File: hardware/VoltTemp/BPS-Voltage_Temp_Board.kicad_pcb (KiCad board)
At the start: 2 copper layers, 98.2 x 56.2 mm, 144 parts, among them IC1 ISO1641BDR, J10 53307-2471, J11 Conn_01x07, J12 Conn_01x04, J13 Conn_01x04, J5 Logic_Analyzer, J6 Conn_01x04, J7 Conn_01x04, J8 Conn_01x06, J9 Conn_01x03, SW1 BOOT, U1 EL3H7, U12 TLV9062xD, U13 TLV9062xD, U14 TLV9062xD, U2 BQ7692003PW, U3 EL3H7, U4 TLV9062xD, U6 TLV9062xD

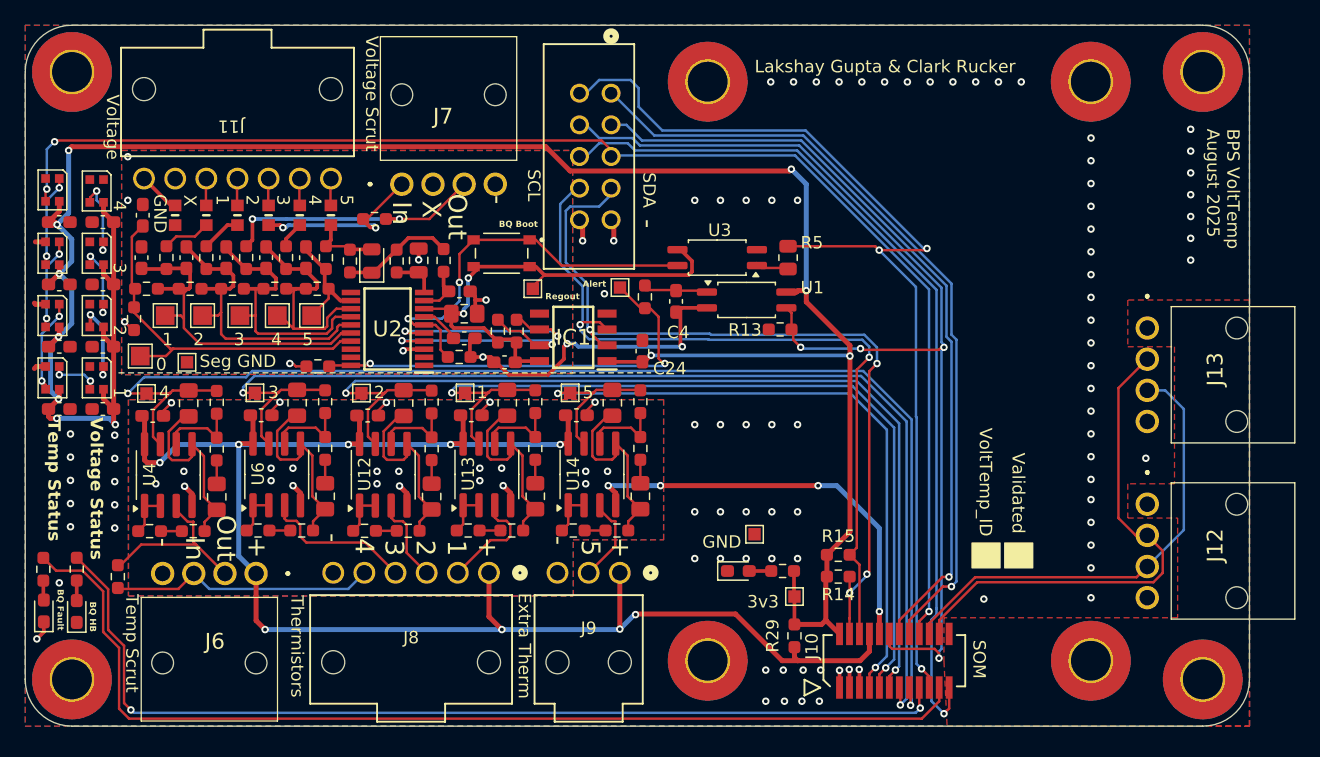
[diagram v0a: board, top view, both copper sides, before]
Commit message: fixed nanofit footprints and add labels to can in can out connectors
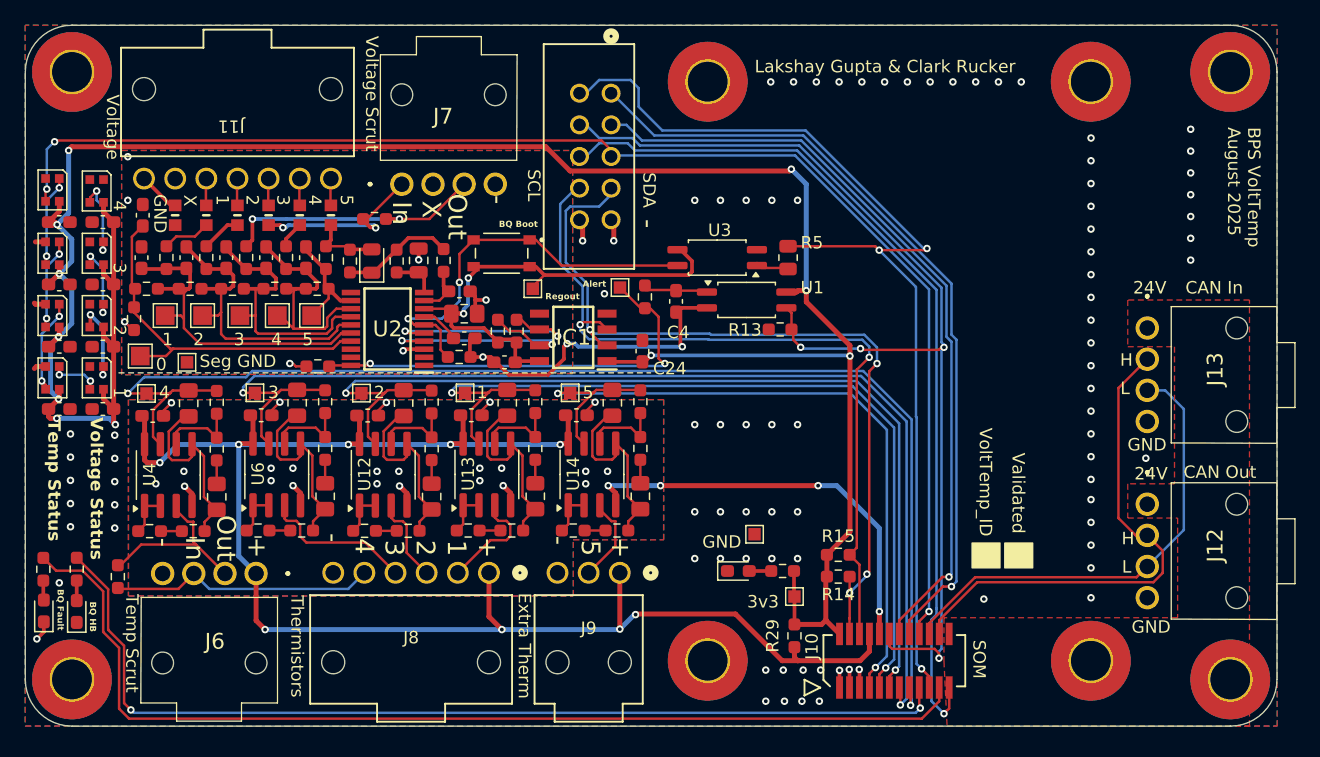
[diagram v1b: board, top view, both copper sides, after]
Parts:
- U2: value BQ7692003PW -> SOP65P640X120-20N
- moved MH4 2.21 mm to (215.0, 69.7)
- moved MH3 2.21 mm to (215.0, 118.4)
- moved LOGO2 0.43 mm to (209.4, 79.2)
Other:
- board size 98.2 x 56.2 mm -> 100.4 x 56.2 mm
- board text added: "24V"
- board text added: "CAN In"
- board text added: "CAN Out"
- board text added: "H"
- board text added: "L"
- board text added: "Todo: - Layout :( [X] - Update constrains [X] - Mirror thermistor flex pinout [X] - Label voltage connector [X] - Fix iso i2c footprint [X] - Make proper edge cuts [X] - Add stitching vias [X] - Update pcb from schematic once schematic todo done [X] - Figure out edge to connector clearance for nanofits [X] - Redo addressable led routing [X] - Verify 24V traces can handle 8 Volttemps of current [X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"
- board text removed: "Todo: - Layout :( [X] - Update constrains [X] - Mirror thermistor flex pinout [X] - Label voltage connector [X] - Fix iso i2c footprint [X] - Make proper edge cuts [X] - Add stitching vias [X] - Update pcb from schematic once schematic todo done [X] - Figure out edge to connector clearance for nanofits [] - Redo addressable led routing [X] - Verify 24V traces can handle 8 Volttemps of current [X]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"

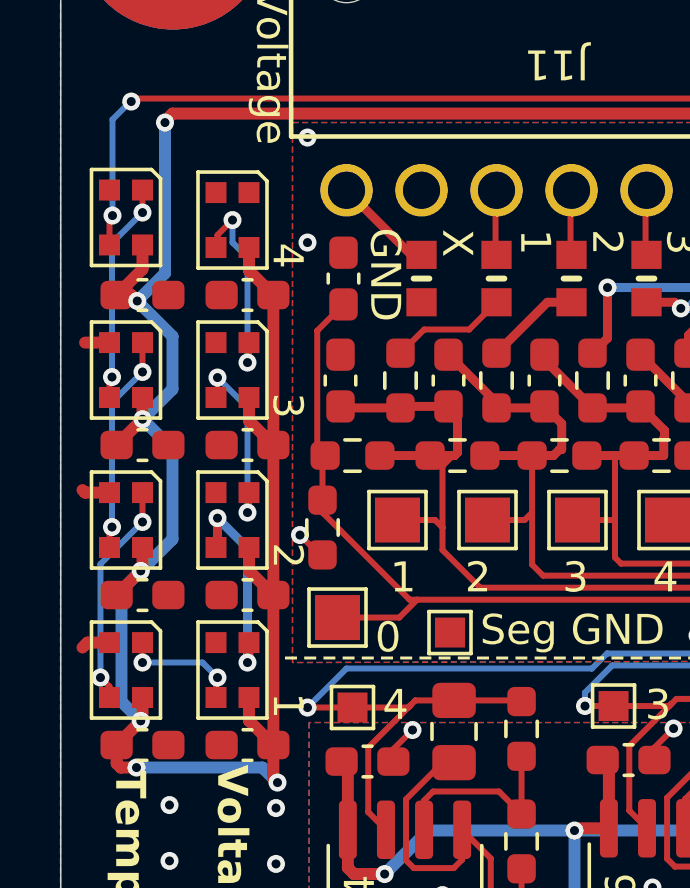
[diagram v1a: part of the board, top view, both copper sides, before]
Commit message: changed bild to sharepoint
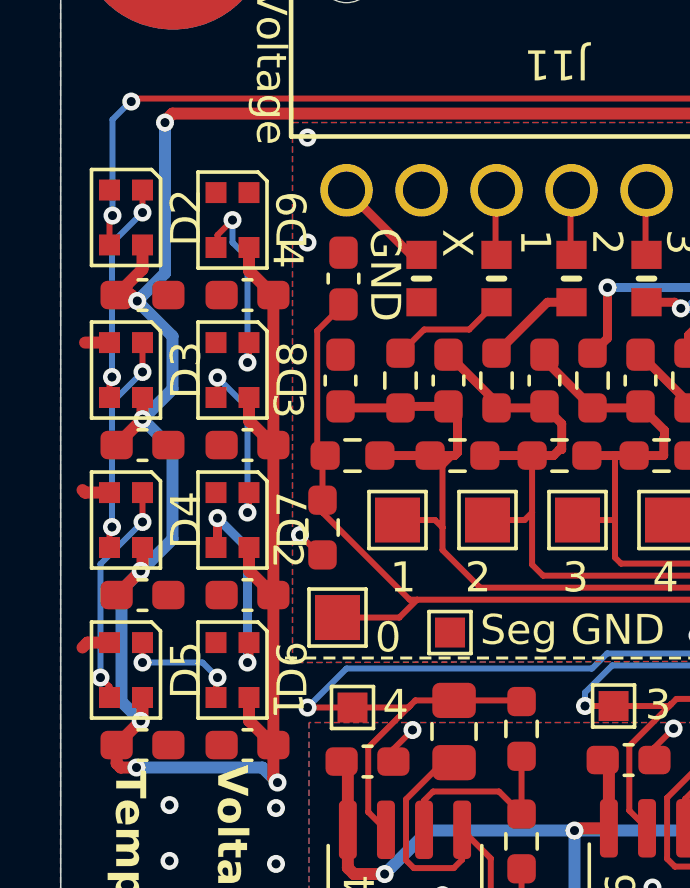
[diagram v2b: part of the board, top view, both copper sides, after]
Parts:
- D2, D3, D4, D5, D6, D7, D8, D9: footprint VoltTemp:WS2812B-2020 -> LED_SMD:LED_WS2812B-2020_PLCC4_2.0x2.0mm
- U2: value SOP65P640X120-20N -> BQ7692003PW
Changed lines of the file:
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@@
 	(net 107 "/BQ_HB")
 	(net 108 "Net-(D10-A)")
+	(net 109 "unconnected-(J10-MNT-Pad28)")
+	(net 110 "unconnected-(J10-MNT-Pad26)")
+	(net 111 "unconnected-(J10-MNT-Pad28)_1")
+	(net 112 "unconnected-(J10-MNT-Pad27)")
+	(net 113 "unconnected-(J10-MNT-Pad27)_2")
+	(net 114 "unconnected-(J10-MNT-Pad25)_1")
+	(net 115 "unconnected-(J10-MNT-Pad26)_2")
+	(net 116 "unconnected-(J10-MNT-Pad25)_2")
+	(net 117 "unconnected-(MH1-Pad1)")
+	(net 118 "unconnected-(MH1-Pad1)_2")
+	(net 119 "unconnected-(MH2-Pad1)_1")
+	(net 120 "unconnected-(MH2-Pad1)_2")
+	(net 121 "unconnected-(MH3-Pad1)")
+	(net 122 "unconnected-(MH3-Pad1)_2")
+	(net 123 "unconnected-(MH4-Pad1)")
+	(net 124 "unconnected-(MH4-Pad1)_1")
 	(footprint "Capacitor_SMD:C_0805_2012Metric_Pad1.18x1.45mm_HandSolder"
 		(layer "F.Cu")
@@
 		)
 	)
-	(footprint "VoltTemp:WS2812B-2020"
+	(footprint "LED_SMD:LED_WS2812B-2020_PLCC4_2.0x2.0mm"
 		(layer "F.Cu")
 		(at 120.45 84.25 -90)
@@
 			(at 0 -2 270)
 			(layer "F.SilkS")
-			(hide yes)
 			(effects
 				(font
@@
 		)
 		(embedded_fonts no)
-		(embedded_files
-			(file
-				(name "WS2812B-2020--3DModel-STEP-269445.STEP")
-				(type model)
-				(checksum "3DF7FEB12B62EBF7ED4E8B8A585F0BB0")
-			)
-		)
-		(model "kicad-embed://WS2812B-2020--3DModel-STEP-269445.STEP"
+		(model "${KICAD9_3DMODEL_DIR}/LED_SMD.3dshapes/LED_WS2812B-2020_PLCC4_2.0x2.0mm.wrl"
 			(offset
 				(xyz 0 0 0)
@@
 			)
 			(rotate
-				(xyz -90 -0 -0)
+				(xyz 0 0 0)
 			)
 		)
@@
 		)
 	)
-	(footprint "VoltTemp:WS2812B-2020"
+	(footprint "LED_SMD:LED_WS2812B-2020_PLCC4_2.0x2.0mm"
 		(layer "F.Cu")
 		(at 124 89.25 -90)
@@
 			(at 0 -2 270)
 			(layer "F.SilkS")
-			(hide yes)
 			(effects
 				(font
@@
 		)
 		(embedded_fonts no)
-		(embedded_files
-			(file
-				(name "WS2812B-2020--3DModel-STEP-269445.STEP")
-				(type model)
-				(checksum "3DF7FEB12B62EBF7ED4E8B8A585F0BB0")
-			)
-		)
-		(model "kicad-embed://WS2812B-2020--3DModel-STEP-269445.STEP"
+		(model "${KICAD9_3DMODEL_DIR}/LED_SMD.3dshapes/LED_WS2812B-2020_PLCC4_2.0x2.0mm.wrl"
 			(offset
 				(xyz 0 0 0)
@@
 			)
 			(rotate
-				(xyz -90 -0 -0)
+				(xyz 0 0 0)
 			)
 		)
@@
 			(size 6.4 6.4)
 			(layers "F.Cu" "F.Mask")
-			(net 103 "unconnected-(MH4-Pad1)_2")
+			(net 124 "unconnected-(MH4-Pad1)_1")
 			(pinfunction "1")
 			(pintype "input+no_connect")
@@
 			(size 6.4 6.4)
 			(layers "B.Cu" "B.Mask")
-			(net 103 "unconnected-(MH4-Pad1)_2")
+			(net 123 "unconnected-(MH4-Pad1)")
 			(pinfunction "1")
 			(pintype "input+no_connect")
@@
 			)
 		)
-		(property "Datasheet" "https://www.lcsc.com/datasheet/C7371904.pdf"
+		(property "Datasheet" ""
 			(at 0 0 0)
 			(unlocked yes)
@@
 		)
 	)
-	(footprint "VoltTemp:WS2812B-2020"
+	(footprint "LED_SMD:LED_WS2812B-2020_PLCC4_2.0x2.0mm"
 		(layer "F.Cu")
 		(at 120.45 89.25 -90)
@@
 			(at 0 -2 270)
 			(layer "F.SilkS")
-			(hide yes)
 			(effects
 				(font
@@
 		)
 		(embedded_fonts no)
-		(embedded_files
-			(file
-				(name "WS2812B-2020--3DModel-STEP-269445.STEP")
-				(type model)
-				(checksum "3DF7FEB12B62EBF7ED4E8B8A585F0BB0")
-			)
-		)
-		(model "kicad-embed://WS2812B-2020--3DModel-STEP-269445.STEP"
+		(model "${KICAD9_3DMODEL_DIR}/LED_SMD.3dshapes/LED_WS2812B-2020_PLCC4_2.0x2.0mm.wrl"
 			(offset
 				(xyz 0 0 0)
@@
 			)
 			(rotate
-				(xyz -90 -0 -0)
+				(xyz 0 0 0)
 			)
 		)
@@
 		(embedded_fonts no)
 	)
-	(footprint "VoltTemp:WS2812B-2020"
+	(footprint "LED_SMD:LED_WS2812B-2020_PLCC4_2.0x2.0mm"
 		(layer "F.Cu")
 		(at 120.45 94.25 -90)
@@
 			(at 0 -2 270)
 			(layer "F.SilkS")
-			(hide yes)
 			(effects
 				(font
@@
 		)
 		(embedded_fonts no)
-		(embedded_files
-			(file
-				(name "WS2812B-2020--3DModel-STEP-269445.STEP")
-				(type model)
-				(checksum "3DF7FEB12B62EBF7ED4E8B8A585F0BB0")
-			)
-		)
-		(model "kicad-embed://WS2812B-2020--3DModel-STEP-269445.STEP"
+		(model "${KICAD9_3DMODEL_DIR}/LED_SMD.3dshapes/LED_WS2812B-2020_PLCC4_2.0x2.0mm.wrl"
 			(offset
 				(xyz 0 0 0)
@@
 			)
 			(rotate
-				(xyz -90 -0 -0)
+				(xyz 0 0 0)
 			)
 		)
@@
 			(size 6.4 6.4)
 			(layers "F.Cu" "F.Mask")
-			(net 90 "unconnected-(J10-MNT-Pad25)")
+			(net 116 "unconnected-(J10-MNT-Pad25)_2")
 			(pinfunction "MNT")
 			(pintype "power_in+no_connect")
@@
 			(size 6.4 6.4)
 			(layers "B.Cu" "B.Mask")
-			(net 90 "unconnected-(J10-MNT-Pad25)")
+			(net 114 "unconnected-(J10-MNT-Pad25)_1")
 			(pinfunction "MNT")
 			(pintype "power_in+no_connect")
@@
 			(layers "*.Cu" "*.Mask")
 			(remove_unused_layers no)
-			(net 91 "unconnected-(J10-MNT-Pad26)_1")
+			(net 110 "unconnected-(J10-MNT-Pad26)")
 			(pinfunction "MNT")
 			(pintype "power_in+no_connect")
@@
 			(size 6.4 6.4)
 			(layers "F.Cu" "F.Mask")
-			(net 91 "unconnected-(J10-MNT-Pad26)_1")
+			(net 115 "unconnected-(J10-MNT-Pad26)_2")
 			(pinfunction "MNT")
 			(pintype "power_in+no_connect")
@@
 			(layers "*.Cu" "*.Mask")
 			(remove_unused_layers no)
-			(net 92 "unconnected-(J10-MNT-Pad27)_1")
+			(net 112 "unconnected-(J10-MNT-Pad27)")
 			(pinfunction "MNT")
 			(pintype "power_in+no_connect")
@@
 			(size 6.4 6.4)
 			(layers "B.Cu" "B.Mask")
-			(net 92 "unconnected-(J10-MNT-Pad27)_1")
+			(net 113 "unconnected-(J10-MNT-Pad27)_2")
 			(pinfunction "MNT")
 			(pintype "power_in+no_connect")
@@
 			(size 6.4 6.4)
 			(layers "F.Cu" "F.Mask")
-			(net 93 "unconnected-(J10-MNT-Pad28)_2")
+			(net 109 "unconnected-(J10-MNT-Pad28)")
 			(pinfunction "MNT")
 			(pintype "power_in+no_connect")
@@
 			(size 6.4 6.4)
 			(layers "B.Cu" "B.Mask")
-			(net 93 "unconnected-(J10-MNT-Pad28)_2")
+			(net 111 "unconnected-(J10-MNT-Pad28)_1")
 			(pinfunction "MNT")
 			(pintype "power_in+no_connect")
@@
 		)
 	)
-	(footprint "VoltTemp:WS2812B-2020"
+	(footprint "LED_SMD:LED_WS2812B-2020_PLCC4_2.0x2.0mm"
 		(layer "F.Cu")
 		(at 124 94.25 -90)
@@
 			(at 0 -2 270)
 			(layer "F.SilkS")
-			(hide yes)
 			(effects
 				(font
@@
 		)
 		(embedded_fonts no)
-		(embedded_files
-			(file
-				(name "WS2812B-2020--3DModel-STEP-269445.STEP")
-				(type model)
-				(checksum "3DF7FEB12B62EBF7ED4E8B8A585F0BB0")
-			)
-		)
-		(model "kicad-embed://WS2812B-2020--3DModel-STEP-269445.STEP"
+		(model "${KICAD9_3DMODEL_DIR}/LED_SMD.3dshapes/LED_WS2812B-2020_PLCC4_2.0x2.0mm.wrl"
 			(offset
 				(xyz 0 0 0)
@@
 			)
 			(rotate
-				(xyz -90 -0 -0)
+				(xyz 0 0 0)
 			)
 		)
@@
 		)
 	)
-	(footprint "VoltTemp:WS2812B-2020"
+	(footprint "LED_SMD:LED_WS2812B-2020_PLCC4_2.0x2.0mm"
 		(layer "F.Cu")
 		(at 124 84.25 -90)
@@
 			(at 0 -2 270)
 			(layer "F.SilkS")
-			(hide yes)
 			(effects
 				(font
@@
 		)
 		(embedded_fonts no)
-		(embedded_files
-			(file
-				(name "WS2812B-2020--3DModel-STEP-269445.STEP")
-				(type model)
-				(checksum "3DF7FEB12B62EBF7ED4E8B8A585F0BB0")
-			)
-		)
-		(model "kicad-embed://WS2812B-2020--3DModel-STEP-269445.STEP"
+		(model "${KICAD9_3DMODEL_DIR}/LED_SMD.3dshapes/LED_WS2812B-2020_PLCC4_2.0x2.0mm.wrl"
 			(offset
 				(xyz 0 0 0)
@@
 			)
 			(rotate
-				(xyz -90 -0 -0)
+				(xyz 0 0 0)
 			)
 		)
@@
 			)
 		)
-		(property "Datasheet" "https://www.lcsc.com/datasheet/C7371904.pdf"
+		(property "Datasheet" ""
 			(at 0 0 90)
 			(unlocked yes)
@@
 		)
 	)
-	(footprint "VoltTemp:WS2812B-2020"
+	(footprint "LED_SMD:LED_WS2812B-2020_PLCC4_2.0x2.0mm"
 		(layer "F.Cu")
 		(at 120.45 79.165 -90)
@@
 			(at 0 -2 270)
 			(layer "F.SilkS")
-			(hide yes)
 			(effects
 				(font
@@
 		)
 		(embedded_fonts no)
-		(embedded_files
-			(file
-				(name "WS2812B-2020--3DModel-STEP-269445.STEP")
-				(type model)
-				(checksum "3DF7FEB12B62EBF7ED4E8B8A585F0BB0")
-			)
-		)
-		(model "kicad-embed://WS2812B-2020--3DModel-STEP-269445.STEP"
+		(model "${KICAD9_3DMODEL_DIR}/LED_SMD.3dshapes/LED_WS2812B-2020_PLCC4_2.0x2.0mm.wrl"
 			(offset
 				(xyz 0 0 0)
@@
 			)
 			(rotate
-				(xyz -90 -0 -0)
+				(xyz 0 0 0)
 			)
 		)
@@
 		)
 	)
-	(footprint "VoltTemp:WS2812B-2020"
+	(footprint "LED_SMD:LED_WS2812B-2020_PLCC4_2.0x2.0mm"
 		(layer "F.Cu")
 		(at 124 79.25 -90)
@@
 			(at 0 -2 270)
 			(layer "F.SilkS")
-			(hide yes)
 			(effects
 				(font
@@
 		)
 		(embedded_fonts no)
-		(embedded_files
-			(file
-				(name "WS2812B-2020--3DModel-STEP-269445.STEP")
-				(type model)
-				(checksum "3DF7FEB12B62EBF7ED4E8B8A585F0BB0")
-			)
-		)
-		(model "kicad-embed://WS2812B-2020--3DModel-STEP-269445.STEP"
+		(model "${KICAD9_3DMODEL_DIR}/LED_SMD.3dshapes/LED_WS2812B-2020_PLCC4_2.0x2.0mm.wrl"
 			(offset
 				(xyz 0 0 0)
@@
 			)
 			(rotate
-				(xyz -90 -0 -0)
+				(xyz 0 0 0)
 			)
 		)
@@
 			(layers "*.Cu" "*.Mask")
 			(remove_unused_layers no)
-			(net 100 "unconnected-(MH1-Pad1)_1")
+			(net 117 "unconnected-(MH1-Pad1)")
 			(pinfunction "1")
 			(pintype "input+no_connect")
@@
 			(size 6.4 6.4)
 			(layers "F.Cu" "F.Mask")
-			(net 100 "unconnected-(MH1-Pad1)_1")
+			(net 118 "unconnected-(MH1-Pad1)_2")
 			(pinfunction "1")
 			(pintype "input+no_connect")
@@
 			(layers "*.Cu" "*.Mask")
 			(remove_unused_layers no)
-			(net 102 "unconnected-(MH3-Pad1)_1")
+			(net 121 "unconnected-(MH3-Pad1)")
 			(pinfunction "1")
 			(pintype "input+no_connect")
@@
 			(size 6.4 6.4)
 			(layers "B.Cu" "B.Mask")
-			(net 102 "unconnected-(MH3-Pad1)_1")
+			(net 122 "unconnected-(MH3-Pad1)_2")
 			(pinfunction "1")
 			(pintype "input+no_connect")
@@
 			)
 		)
-		(property "Datasheet" "https://www.lcsc.com/datasheet/C7371904.pdf"
+		(property "Datasheet" ""
 			(at 0 0 90)
 			(unlocked yes)
@@
 			(size 6.4 6.4)
 			(layers "F.Cu" "F.Mask")
-			(net 101 "unconnected-(MH2-Pad1)")
+			(net 119 "unconnected-(MH2-Pad1)_1")
 			(pinfunction "1")
 			(pintype "input+no_connect")
@@
 			(size 6.4 6.4)
 			(layers "B.Cu" "B.Mask")
-			(net 101 "unconnected-(MH2-Pad1)")
+			(net 120 "unconnected-(MH2-Pad1)_2")
 			(pinfunction "1")
 			(pintype "input+no_connect")
@@
 			)
 		)
-		(property "Value" "SOP65P640X120-20N"
+		(property "Value" "BQ7692003PW"
 			(at 0 0 0)
 			(layer "F.SilkS")

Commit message: ravi shah
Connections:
- F12 pad 2: GND2 -> GND_Seg
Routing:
- net GND_Seg: track 34.0 -> 34.7 mm, vias 10 -> 25
- net GNDA: vias 27 -> 28
- net GND: vias 88 -> 86
